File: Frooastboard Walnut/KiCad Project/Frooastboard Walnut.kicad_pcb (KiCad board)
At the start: 2 copper layers, 357.2 x 100 mm, 172 parts, among them SW1 SW_Push, U1 ATmega32U4-A, Y1 Crystal_GND24_Small

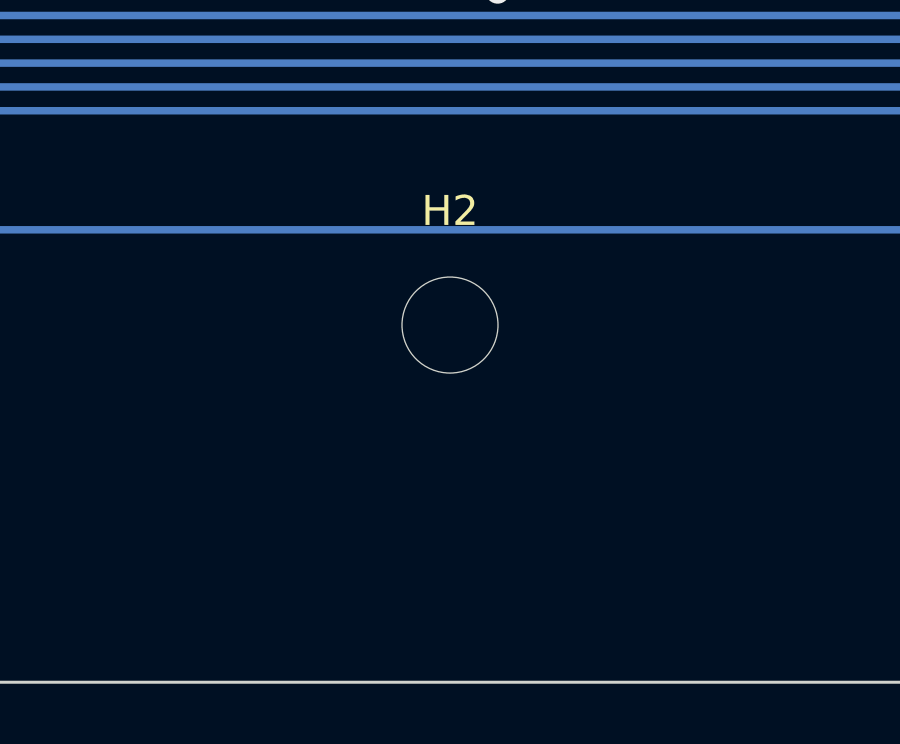
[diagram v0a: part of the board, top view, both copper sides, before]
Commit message: Move screw hole
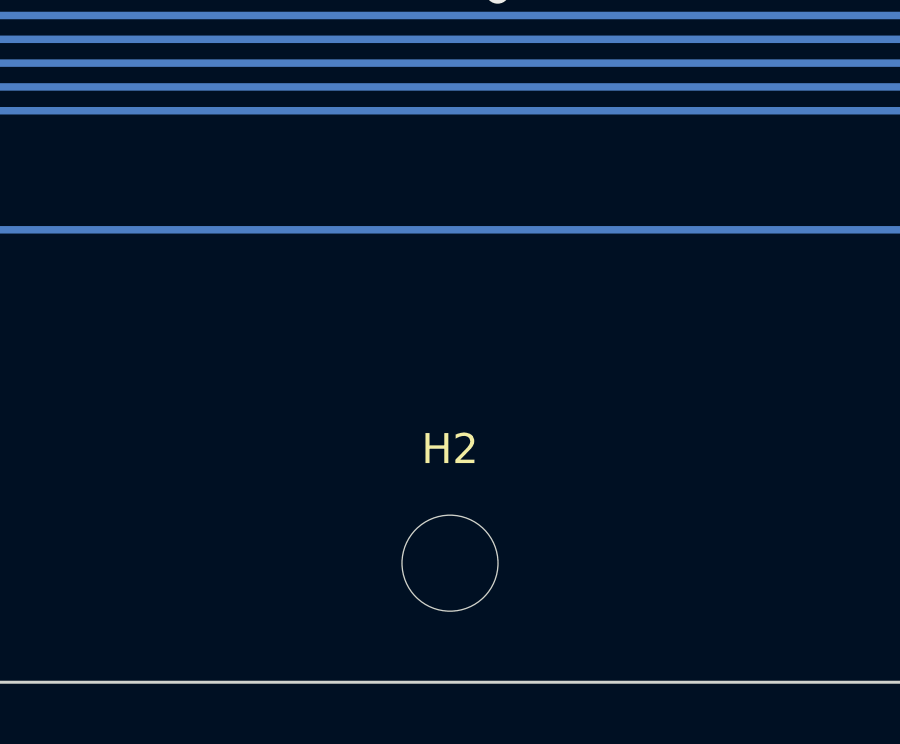
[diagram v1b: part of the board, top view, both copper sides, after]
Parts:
- moved H2 7.94 mm to (127.8, 115.1)
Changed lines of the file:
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@@
   )
   (footprint "MountingHole:MountingHole_3.2mm_M3_DIN965" (layer "F.Cu")
-    (at 127.79375 107.15625)
+    (at 127.79375 115.09375)
     (descr "Mounting Hole 3.2mm, no annular, M3, DIN965")
     (tags "mounting hole 3.2mm no annular m3 din965")

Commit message: rotate iso enter switch
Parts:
- KEY_ENTER1: footprint MX_Only:MXOnly-ISO-NoLED-NoStabilizers -> MX_Only:MXOnly-ISO-ROTATED-NoLED-NoStabilizers
- moved D52 10.6 mm to (303.9, 64.3), turned to 180 degrees
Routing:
- net Net-(D52-Pad2): track 27.0 -> 18.3 mm
- net COL5: track 428.3 -> 434.5 mm
- net ROW3: track 216.7 -> 219.9 mm

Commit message: Mounting Holes
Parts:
- removed FID1, FID2: Fiducial, Fiducial:Fiducial_1mm_Mask2mm
- added H10: MountingHole, MountingHole:MountingHole_3.2mm_M3_DIN965, F.Cu at (211.9, 22.2)
- added H11: MountingHole, MountingHole:MountingHole_3.2mm_M3_DIN965, F.Cu at (116.7, 22.2)
- added H12: MountingHole, MountingHole:MountingHole_3.2mm_M3_DIN965, F.Cu at (354.8, 22.2)
- added H13: MountingHole, MountingHole:MountingHole_3.2mm_M3_DIN965, F.Cu at (177.0, 115.9)
- added H5: MountingHole, MountingHole:MountingHole_3.2mm_M3_DIN965, F.Cu at (354.8, 115.9)
- added H6: MountingHole, MountingHole:MountingHole_3.2mm_M3_DIN965, F.Cu at (40.5, 22.2)
- added H7: MountingHole, MountingHole:MountingHole_3.2mm_M3_DIN965, F.Cu at (45.2, 115.9)
- added H8: MountingHole, MountingHole:MountingHole_3.2mm_M3_DIN965, F.Cu at (259.6, 115.9)
- added H9: MountingHole, MountingHole:MountingHole_3.2mm_M3_DIN965, F.Cu at (173.8, 22.2)
- moved H3 42.9 mm to (269.1, 22.2)
- moved H4 21.0 mm to (373.1, 69.1)
- moved H1 2.38 mm to (22.2, 69.1)
- moved H2 0.79 mm to (127.8, 115.9)
